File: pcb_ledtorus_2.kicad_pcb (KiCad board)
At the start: 4 copper layers, 149 x 149 mm, 277 parts, among them P1 CONN_02X04, P2 CONN_6, P3 MICRO-SD, P4 CONN_2, P5 KNUSB, P6 CONN_12, U1 STM32F46X_LQFP176, U10 TLC5955, U11 TLC5955, U12 TLC5955, U13 TLC5955, U14 TLC5955, U15 TLC5955, U3 LP38691, U4 TLC5955, U5 TLC5955, U6 TLC5955, U7 TLC5955, U8 TLC5955, U9 TLC5955, X1 MA-505

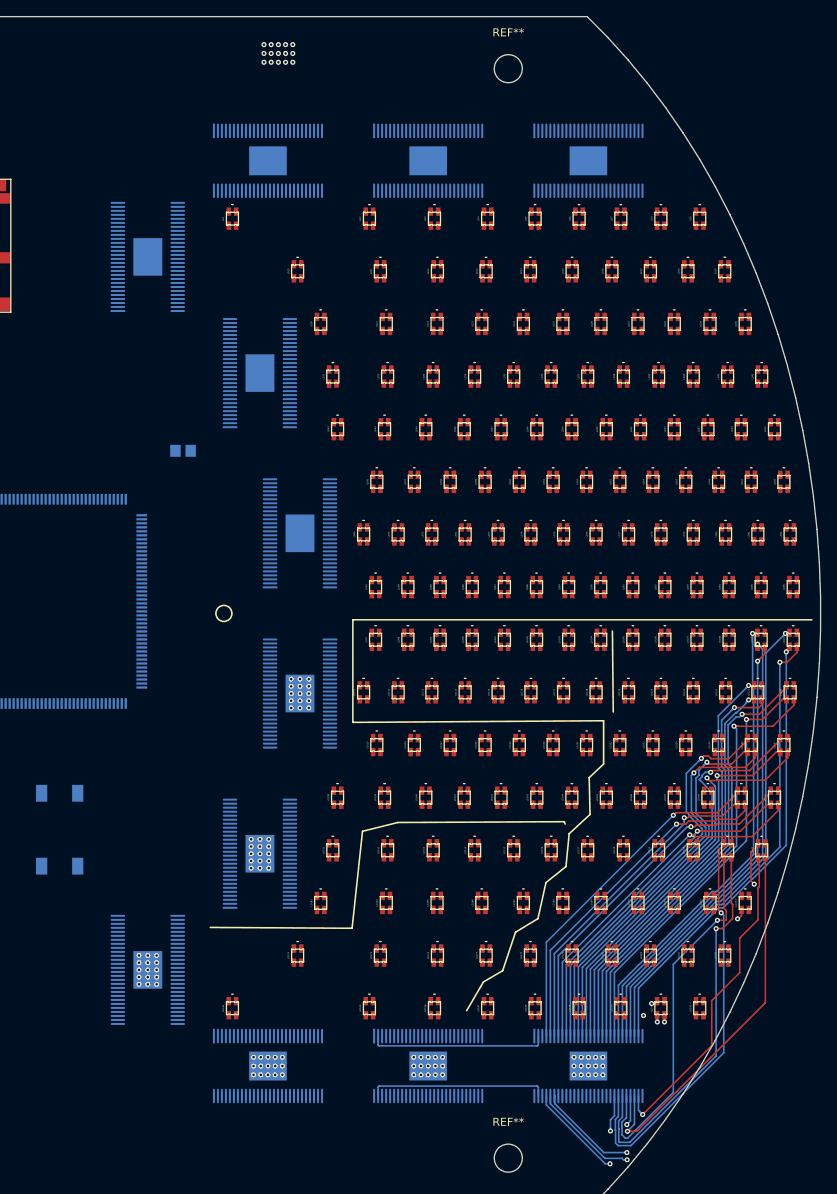
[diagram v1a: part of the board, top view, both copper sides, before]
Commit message: Good progress on LED routing.
Upper half now routed with 6/6 mil tracks/clearance.
Still need to fit 5V vias for all LEDs, hopefully vias can find room.
Looks promising - if everything works, lower half should be doable the
same way.
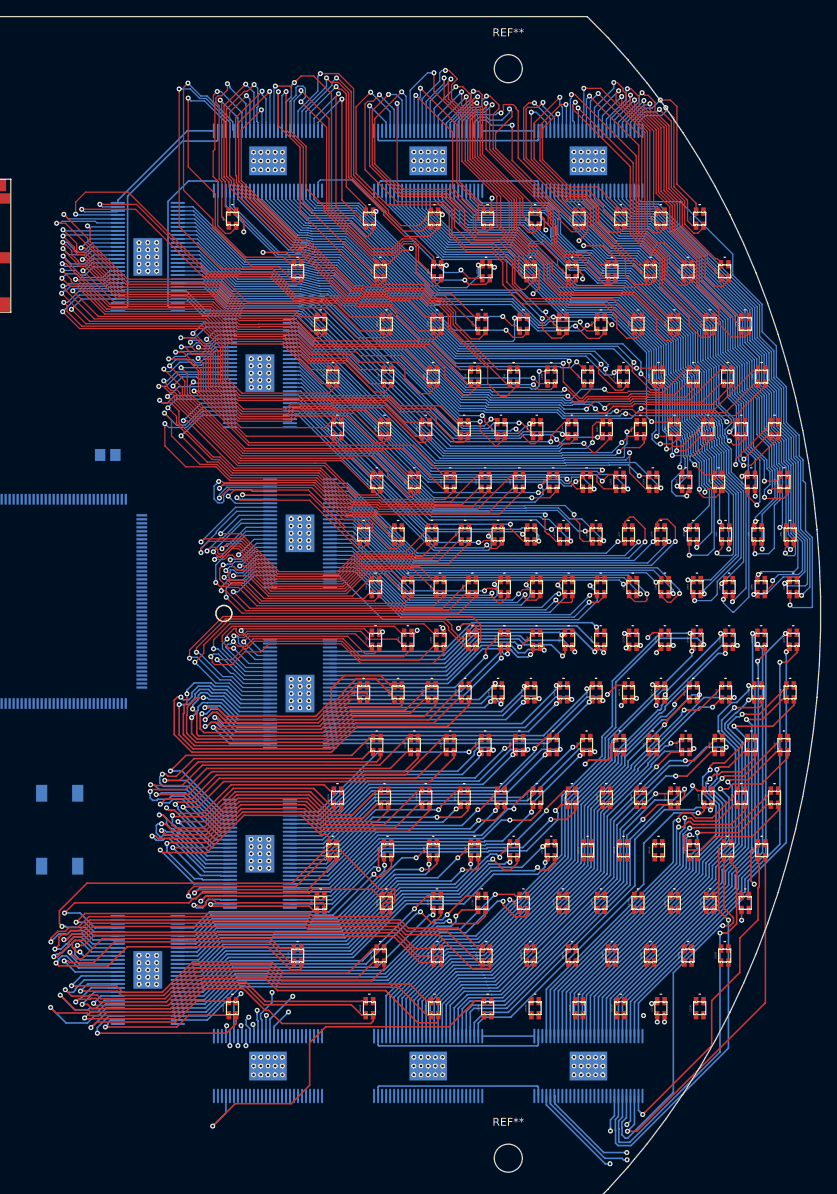
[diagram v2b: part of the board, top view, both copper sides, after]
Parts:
- moved C36 9.41 mm to (135.5, 130.2)
- turned U11 to 270 degrees
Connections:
- U11 pad 10: /LEDs/led140b -> /LEDs/led130b
- U11 pad 11: /LEDs/led140r -> /LEDs/led130r
- U11 pad 12: /LEDs/led140g -> /LEDs/led130g
- U11 pad 13: /LEDs/led139b -> /LEDs/led131b
- U11 pad 14: /LEDs/led139r -> /LEDs/led131r
- U11 pad 15: /LEDs/led139g -> /LEDs/led131g
- U11 pad 16: /LEDs/led138b -> /LEDs/led141b
- U11 pad 17: /LEDs/led138r -> /LEDs/led141r
- U11 pad 18: /LEDs/led138g -> /LEDs/led141g
- U11 pad 19: /LEDs/led127b -> /LEDs/led142b
- U11 pad 20: /LEDs/led127r -> /LEDs/led142r
- U11 pad 21: /LEDs/led127g -> /LEDs/led142g
- U11 pad 22: /LEDs/led126b -> /LEDs/led143b
- U11 pad 23: /LEDs/led126r -> /LEDs/led143r
- U11 pad 24: /LEDs/led126g -> /LEDs/led143g
- U11 pad 25: /LEDs/led125b -> /LEDs/led144b
- U11 pad 26: /LEDs/led125r -> /LEDs/led144r
- U11 pad 27: /LEDs/led125g -> /LEDs/led144g
- U11 pad 30: /LEDs/led128g -> /LEDs/led163g
- U11 pad 31: /LEDs/led128r -> /LEDs/led163r
- U11 pad 32: /LEDs/led128b -> /LEDs/led163b
- U11 pad 33: /LEDs/led129g -> /LEDs/led151g
- U11 pad 34: /LEDs/led129r -> /LEDs/led151r
- U11 pad 35: /LEDs/led129b -> /LEDs/led151b
- U11 pad 36: /LEDs/led130g -> /LEDs/led140g
- U11 pad 37: /LEDs/led130r -> /LEDs/led140r
- U11 pad 38: /LEDs/led130b -> /LEDs/led140b
- U11 pad 39: /LEDs/led131g -> /LEDs/led139g
- U11 pad 4: /LEDs/led163b -> /LEDs/led128b
- U11 pad 40: /LEDs/led131r -> /LEDs/led139r
- U11 pad 41: /LEDs/led131b -> /LEDs/led139b
- U11 pad 42: /LEDs/led141g -> /LEDs/led138g
- U11 pad 43: /LEDs/led141r -> /LEDs/led138r
- U11 pad 44: /LEDs/led141b -> /LEDs/led138b
- U11 pad 45: /LEDs/led142g -> /LEDs/led127g
- U11 pad 46: /LEDs/led142r -> /LEDs/led127r
- U11 pad 47: /LEDs/led142b -> /LEDs/led127b
- U11 pad 48: /LEDs/led143g -> /LEDs/led126g
- U11 pad 49: /LEDs/led143r -> /LEDs/led126r
- U11 pad 5: /LEDs/led163r -> /LEDs/led128r
- U11 pad 50: /LEDs/led143b -> /LEDs/led126b
- U11 pad 51: /LEDs/led144g -> /LEDs/led125g
- U11 pad 52: /LEDs/led144r -> /LEDs/led125r
- U11 pad 53: /LEDs/led144b -> /LEDs/led125b
- U11 pad 6: /LEDs/led163g -> /LEDs/led128g
- U11 pad 7: /LEDs/led151b -> /LEDs/led129b
- U11 pad 8: /LEDs/led151r -> /LEDs/led129r
- U11 pad 9: /LEDs/led151g -> /LEDs/led129g
- U12 pad 30: /LEDs/led186g -> /LEDs/led184g
- U12 pad 31: /LEDs/led186r -> /LEDs/led184r
- U12 pad 32: /LEDs/led186b -> /LEDs/led184b
- U12 pad 36: /LEDs/led184g -> /LEDs/led186g
- U12 pad 37: /LEDs/led184r -> /LEDs/led186r
- U12 pad 38: /LEDs/led184b -> /LEDs/led186b
- U12 pad 39: /LEDs/led174g -> /LEDs/led175g
- U12 pad 40: /LEDs/led174r -> /LEDs/led175r
- U12 pad 41: /LEDs/led174b -> /LEDs/led175b
- U12 pad 42: /LEDs/led175g -> /LEDs/led174g
- U12 pad 43: /LEDs/led175r -> /LEDs/led174r
- U12 pad 44: /LEDs/led175b -> /LEDs/led174b
- U13 pad 10: /LEDs/led132b -> /LEDs/led119b
- U13 pad 11: /LEDs/led132r -> /LEDs/led119r
- U13 pad 12: /LEDs/led132g -> /LEDs/led119g
- U13 pad 13: /LEDs/led133b -> /LEDs/led120b
- U13 pad 14: /LEDs/led133r -> /LEDs/led120r
- U13 pad 15: /LEDs/led133g -> /LEDs/led120g
- U13 pad 16: /LEDs/led119b -> /LEDs/led132b
- U13 pad 17: /LEDs/led119r -> /LEDs/led132r
- U13 pad 18: /LEDs/led119g -> /LEDs/led132g
- U13 pad 19: /LEDs/led120b -> /LEDs/led133b
- U13 pad 20: /LEDs/led120r -> /LEDs/led133r
- U13 pad 21: /LEDs/led120g -> /LEDs/led133g
- U13 pad 22: /LEDs/led105b -> /LEDs/led145b
- U13 pad 23: /LEDs/led105r -> /LEDs/led145r
- U13 pad 24: /LEDs/led105g -> /LEDs/led145g
- U13 pad 25: /LEDs/led106b -> /LEDs/led146b
- U13 pad 26: /LEDs/led106r -> /LEDs/led146r
- U13 pad 27: /LEDs/led106g -> /LEDs/led146g
- U13 pad 4: /LEDs/led145b -> /LEDs/led105b
- U13 pad 5: /LEDs/led145r -> /LEDs/led105r
- U13 pad 6: /LEDs/led145g -> /LEDs/led105g
- U13 pad 7: /LEDs/led146b -> /LEDs/led106b
- U13 pad 8: /LEDs/led146r -> /LEDs/led106r
- U13 pad 9: /LEDs/led146g -> /LEDs/led106g
- U14 pad 10: /LEDs/led134b -> /LEDs/led121b
- U14 pad 11: /LEDs/led134r -> /LEDs/led121r
- U14 pad 12: /LEDs/led134g -> /LEDs/led121g
- U14 pad 13: /LEDs/led135b -> /LEDs/led122b
- U14 pad 14: /LEDs/led135r -> /LEDs/led122r
- U14 pad 15: /LEDs/led135g -> /LEDs/led122g
- U14 pad 16: /LEDs/led121b -> /LEDs/led134b
- U14 pad 17: /LEDs/led121r -> /LEDs/led134r
- U14 pad 18: /LEDs/led121g -> /LEDs/led134g
- U14 pad 19: /LEDs/led122b -> /LEDs/led135b
- U14 pad 20: /LEDs/led122r -> /LEDs/led135r
- U14 pad 21: /LEDs/led122g -> /LEDs/led135g
- U14 pad 22: /LEDs/led107b -> /LEDs/led147b
- U14 pad 23: /LEDs/led107r -> /LEDs/led147r
- U14 pad 24: /LEDs/led107g -> /LEDs/led147g
- U14 pad 25: /LEDs/led108b -> /LEDs/led148b
- U14 pad 26: /LEDs/led108r -> /LEDs/led148r
- U14 pad 27: /LEDs/led108g -> /LEDs/led148g
- U14 pad 4: /LEDs/led147b -> /LEDs/led107b
- U14 pad 5: /LEDs/led147r -> /LEDs/led107r
- U14 pad 6: /LEDs/led147g -> /LEDs/led107g
- U14 pad 7: /LEDs/led148b -> /LEDs/led108b
- U14 pad 8: /LEDs/led148r -> /LEDs/led108r
- U14 pad 9: /LEDs/led148g -> /LEDs/led108g
- U4 pad 10: /LEDs/led3b -> /LEDs/led4b
- U4 pad 11: /LEDs/led3r -> /LEDs/led4r
- U4 pad 12: /LEDs/led3g -> /LEDs/led4g
- U4 pad 13: /LEDs/led4b -> /LEDs/led28b
- U4 pad 14: /LEDs/led4r -> /LEDs/led28r
- U4 pad 15: /LEDs/led4g -> /LEDs/led28g
- U4 pad 16: /LEDs/led5b -> /LEDs/led15b
- U4 pad 17: /LEDs/led5r -> /LEDs/led15r
- U4 pad 18: /LEDs/led5g -> /LEDs/led15g
- U4 pad 19: /LEDs/led6b -> /LEDs/led5b
- U4 pad 20: /LEDs/led6r -> /LEDs/led5r
- U4 pad 21: /LEDs/led6g -> /LEDs/led5g
- U4 pad 22: /LEDs/led7b -> /LEDs/led16b
- U4 pad 23: /LEDs/led7r -> /LEDs/led16r
- U4 pad 24: /LEDs/led7g -> /LEDs/led16g
- U4 pad 25: /LEDs/led8b -> /LEDs/led6b
- U4 pad 26: /LEDs/led8r -> /LEDs/led6r
- U4 pad 27: /LEDs/led8g -> /LEDs/led6g
- U4 pad 30: /LEDs/led16g -> /LEDs/led94g
- U4 pad 31: /LEDs/led16r -> /LEDs/led94r
- U4 pad 32: /LEDs/led16b -> /LEDs/led94b
- U4 pad 33: /LEDs/led15g -> /LEDs/led93g
- U4 pad 34: /LEDs/led15r -> /LEDs/led93r
- U4 pad 35: /LEDs/led15b -> /LEDs/led93b
- U4 pad 36: /LEDs/led14g -> /LEDs/led80g
- U4 pad 37: /LEDs/led14r -> /LEDs/led80r
- U4 pad 38: /LEDs/led14b -> /LEDs/led80b
- U4 pad 39: /LEDs/led13g -> /LEDs/led79g
- U4 pad 4: /LEDs/led1b -> /LEDs/led27b
- U4 pad 40: /LEDs/led13r -> /LEDs/led79r
- U4 pad 41: /LEDs/led13b -> /LEDs/led79b
- U4 pad 42: /LEDs/led12g -> /LEDs/led66g
- U4 pad 43: /LEDs/led12r -> /LEDs/led66r
- U4 pad 44: /LEDs/led12b -> /LEDs/led66b
- U4 pad 45: /LEDs/led11g -> /LEDs/led65g
- U4 pad 46: /LEDs/led11r -> /LEDs/led65r
- U4 pad 47: /LEDs/led11b -> /LEDs/led65b
- U4 pad 48: /LEDs/led10g -> /LEDs/led53g
- U4 pad 49: /LEDs/led10r -> /LEDs/led53r
- U4 pad 5: /LEDs/led1r -> /LEDs/led27r
- U4 pad 50: /LEDs/led10b -> /LEDs/led53b
- U4 pad 51: /LEDs/led9g -> /LEDs/led52g
- U4 pad 52: /LEDs/led9r -> /LEDs/led52r
- U4 pad 53: /LEDs/led9b -> /LEDs/led52b
- U4 pad 6: /LEDs/led1g -> /LEDs/led27g
- U4 pad 7: /LEDs/led2b -> /LEDs/led14b
- U4 pad 8: /LEDs/led2r -> /LEDs/led14r
- U4 pad 9: /LEDs/led2g -> /LEDs/led14g
- U5 pad 10: /LEDs/led16b -> /LEDs/led29b
- U5 pad 11: /LEDs/led16r -> /LEDs/led29r
- U5 pad 12: /LEDs/led16g -> /LEDs/led29g
- U5 pad 13: /LEDs/led7b -> /LEDs/led18b
- U5 pad 14: /LEDs/led7r -> /LEDs/led18r
- U5 pad 15: /LEDs/led7g -> /LEDs/led18g
- U5 pad 16: /LEDs/led17b -> /LEDs/led8b
- U5 pad 17: /LEDs/led17r -> /LEDs/led8r
- U5 pad 18: /LEDs/led17g -> /LEDs/led8g
- U5 pad 19: /LEDs/led18b -> /LEDs/led30b
- U5 pad 20: /LEDs/led18r -> /LEDs/led30r
- U5 pad 21: /LEDs/led18g -> /LEDs/led30g
- U5 pad 22: /LEDs/led9b -> /LEDs/led19b
- U5 pad 23: /LEDs/led9r -> /LEDs/led19r
- U5 pad 24: /LEDs/led9g -> /LEDs/led19g
- U5 pad 25: /LEDs/led19b -> /LEDs/led9b
- U5 pad 26: /LEDs/led19r -> /LEDs/led9r
- U5 pad 27: /LEDs/led19g -> /LEDs/led9g
- U5 pad 30: /LEDs/led42g -> /LEDs/led96g
- U5 pad 31: /LEDs/led42r -> /LEDs/led96r
- U5 pad 32: /LEDs/led42b -> /LEDs/led96b
- U5 pad 33: /LEDs/led30g -> /LEDs/led95g
- U5 pad 34: /LEDs/led30r -> /LEDs/led95r
- U5 pad 35: /LEDs/led30b -> /LEDs/led95b
- U5 pad 36: /LEDs/led41g -> /LEDs/led82g
- U5 pad 37: /LEDs/led41r -> /LEDs/led82r
- U5 pad 38: /LEDs/led41b -> /LEDs/led82b
- U5 pad 39: /LEDs/led29g -> /LEDs/led81g
- U5 pad 4: /LEDs/led15b -> /LEDs/led17b
- U5 pad 40: /LEDs/led29r -> /LEDs/led81r
- U5 pad 41: /LEDs/led29b -> /LEDs/led81b
- U5 pad 42: /LEDs/led40g -> /LEDs/led68g
- U5 pad 43: /LEDs/led40r -> /LEDs/led68r
- U5 pad 44: /LEDs/led40b -> /LEDs/led68b
- U5 pad 45: /LEDs/led28g -> /LEDs/led67g
- U5 pad 46: /LEDs/led28r -> /LEDs/led67r
- U5 pad 47: /LEDs/led28b -> /LEDs/led67b
- U5 pad 48: /LEDs/led39g -> /LEDs/led55g
- U5 pad 49: /LEDs/led39r -> /LEDs/led55r
- U5 pad 5: /LEDs/led15r -> /LEDs/led17r
- U5 pad 50: /LEDs/led39b -> /LEDs/led55b
- U5 pad 51: /LEDs/led27g -> /LEDs/led54g
- U5 pad 52: /LEDs/led27r -> /LEDs/led54r
- U5 pad 53: /LEDs/led27b -> /LEDs/led54b
- U5 pad 6: /LEDs/led15g -> /LEDs/led17g
- U5 pad 7: /LEDs/led6b -> /LEDs/led7b
- U5 pad 8: /LEDs/led6r -> /LEDs/led7r
- U5 pad 9: /LEDs/led6g -> /LEDs/led7g
- U6 pad 10: /LEDs/led35b -> /LEDs/led32b
- U6 pad 11: /LEDs/led35r -> /LEDs/led32r
- U6 pad 12: /LEDs/led35g -> /LEDs/led32g
- U6 pad 13: /LEDs/led36b -> /LEDs/led33b
- U6 pad 14: /LEDs/led36r -> /LEDs/led33r
- U6 pad 15: /LEDs/led36g -> /LEDs/led33g
- U6 pad 16: /LEDs/led37b -> /LEDs/led34b
- U6 pad 17: /LEDs/led37r -> /LEDs/led34r
- U6 pad 18: /LEDs/led37g -> /LEDs/led34g
- U6 pad 19: /LEDs/led38b -> /LEDs/led20b
- U6 pad 20: /LEDs/led38r -> /LEDs/led20r
- U6 pad 21: /LEDs/led38g -> /LEDs/led20g
- U6 pad 22: /LEDs/led39b -> /LEDs/led21b
- U6 pad 23: /LEDs/led39r -> /LEDs/led21r
- U6 pad 24: /LEDs/led39g -> /LEDs/led21g
- U6 pad 25: /LEDs/led40b -> /LEDs/led22b
- U6 pad 26: /LEDs/led40r -> /LEDs/led22r
- U6 pad 27: /LEDs/led40g -> /LEDs/led22g
- U6 pad 30: /LEDs/led48g -> /LEDs/led40g
- U6 pad 31: /LEDs/led48r -> /LEDs/led40r
- U6 pad 32: /LEDs/led48b -> /LEDs/led40b
- U6 pad 33: /LEDs/led47g -> /LEDs/led41g
- U6 pad 34: /LEDs/led47r -> /LEDs/led41r
- U6 pad 35: /LEDs/led47b -> /LEDs/led41b
- U6 pad 36: /LEDs/led46g -> /LEDs/led42g
- U6 pad 37: /LEDs/led46r -> /LEDs/led42r
- U6 pad 38: /LEDs/led46b -> /LEDs/led42b
- U6 pad 39: /LEDs/led45g -> /LEDs/led47g
- U6 pad 4: /LEDs/led31b -> /LEDs/led46b
- U6 pad 40: /LEDs/led45r -> /LEDs/led47r
- U6 pad 41: /LEDs/led45b -> /LEDs/led47b
- U6 pad 42: /LEDs/led44g -> /LEDs/led48g
- U6 pad 43: /LEDs/led44r -> /LEDs/led48r
- U6 pad 44: /LEDs/led44b -> /LEDs/led48b
- U6 pad 45: /LEDs/led43g -> /LEDs/led49g
- U6 pad 46: /LEDs/led43r -> /LEDs/led49r
- U6 pad 47: /LEDs/led43b -> /LEDs/led49b
- U6 pad 48: /LEDs/led42g -> /LEDs/led50g
- U6 pad 49: /LEDs/led42r -> /LEDs/led50r
- U6 pad 5: /LEDs/led31r -> /LEDs/led46r
- U6 pad 50: /LEDs/led42b -> /LEDs/led50b
- U6 pad 51: /LEDs/led41g -> /LEDs/led51g
- U6 pad 52: /LEDs/led41r -> /LEDs/led51r
- U6 pad 53: /LEDs/led41b -> /LEDs/led51b
- U6 pad 6: /LEDs/led31g -> /LEDs/led46g
- U6 pad 7: /LEDs/led34b -> /LEDs/led31b
- U6 pad 8: /LEDs/led34r -> /LEDs/led31r
- U6 pad 9: /LEDs/led34g -> /LEDs/led31g
- U7 pad 10: /LEDs/led51b -> /LEDs/led35b
- U7 pad 11: /LEDs/led51r -> /LEDs/led35r
- U7 pad 12: /LEDs/led51g -> /LEDs/led35g
- U7 pad 13: /LEDs/led52b -> /LEDs/led23b
- U7 pad 14: /LEDs/led52r -> /LEDs/led23r
- U7 pad 15: /LEDs/led52g -> /LEDs/led23g
- U7 pad 16: /LEDs/led53b -> /LEDs/led11b
- U7 pad 17: /LEDs/led53r -> /LEDs/led11r
- U7 pad 18: /LEDs/led53g -> /LEDs/led11g
- U7 pad 19: /LEDs/led54b -> /LEDs/led12b
- U7 pad 20: /LEDs/led54r -> /LEDs/led12r
- U7 pad 21: /LEDs/led54g -> /LEDs/led12g
- U7 pad 22: /LEDs/led55b -> /LEDs/led3b
- U7 pad 23: /LEDs/led55r -> /LEDs/led3r
- U7 pad 24: /LEDs/led55g -> /LEDs/led3g
- U7 pad 25: /LEDs/led56b -> /LEDs/led2b
- U7 pad 26: /LEDs/led56r -> /LEDs/led2r
- U7 pad 27: /LEDs/led56g -> /LEDs/led2g
- U7 pad 30: /LEDs/led64g -> /LEDs/led13g
- U7 pad 31: /LEDs/led64r -> /LEDs/led13r
- U7 pad 32: /LEDs/led64b -> /LEDs/led13b
- U7 pad 33: /LEDs/led63g -> /LEDs/led25g
- U7 pad 34: /LEDs/led63r -> /LEDs/led25r
- U7 pad 35: /LEDs/led63b -> /LEDs/led25b
- U7 pad 36: /LEDs/led62g -> /LEDs/led26g
- U7 pad 37: /LEDs/led62r -> /LEDs/led26r
- U7 pad 38: /LEDs/led62b -> /LEDs/led26b
- U7 pad 39: /LEDs/led61g -> /LEDs/led24g
- U7 pad 4: /LEDs/led49b -> /LEDs/led10b
- U7 pad 40: /LEDs/led61r -> /LEDs/led24r
- U7 pad 41: /LEDs/led61b -> /LEDs/led24b
- U7 pad 42: /LEDs/led60g -> /LEDs/led39g
- U7 pad 43: /LEDs/led60r -> /LEDs/led39r
- U7 pad 44: /LEDs/led60b -> /LEDs/led39b
- U7 pad 45: /LEDs/led59g -> /LEDs/led38g
- U7 pad 46: /LEDs/led59r -> /LEDs/led38r
- U7 pad 47: /LEDs/led59b -> /LEDs/led38b
- U7 pad 48: /LEDs/led58g -> /LEDs/led37g
- U7 pad 49: /LEDs/led58r -> /LEDs/led37r
- U7 pad 5: /LEDs/led49r -> /LEDs/led10r
- U7 pad 50: /LEDs/led58b -> /LEDs/led37b
- U7 pad 51: /LEDs/led57g -> /LEDs/led36g
- U7 pad 52: /LEDs/led57r -> /LEDs/led36r
- U7 pad 53: /LEDs/led57b -> /LEDs/led36b
- U7 pad 6: /LEDs/led49g -> /LEDs/led10g
- U7 pad 7: /LEDs/led50b -> /LEDs/led1b
- U7 pad 8: /LEDs/led50r -> /LEDs/led1r
- U7 pad 9: /LEDs/led50g -> /LEDs/led1g
- U8 pad 10: /LEDs/led67b -> /LEDs/led84b
- U8 pad 11: /LEDs/led67r -> /LEDs/led84r
- U8 pad 12: /LEDs/led67g -> /LEDs/led84g
- U8 pad 13: /LEDs/led68b -> /LEDs/led85b
- U8 pad 14: /LEDs/led68r -> /LEDs/led85r
- U8 pad 15: /LEDs/led68g -> /LEDs/led85g
- U8 pad 16: /LEDs/led69b -> /LEDs/led72b
- U8 pad 17: /LEDs/led69r -> /LEDs/led72r
- U8 pad 18: /LEDs/led69g -> /LEDs/led72g
- U8 pad 19: /LEDs/led70b -> /LEDs/led71b
- U8 pad 20: /LEDs/led70r -> /LEDs/led71r
- U8 pad 21: /LEDs/led70g -> /LEDs/led71g
- U8 pad 22: /LEDs/led71b -> /LEDs/led69b
- U8 pad 23: /LEDs/led71r -> /LEDs/led69r
- U8 pad 24: /LEDs/led71g -> /LEDs/led69g
- U8 pad 25: /LEDs/led72b -> /LEDs/led70b
- U8 pad 26: /LEDs/led72r -> /LEDs/led70r
- U8 pad 27: /LEDs/led72g -> /LEDs/led70g
- U8 pad 30: /LEDs/led80g -> /LEDs/led77g
- U8 pad 31: /LEDs/led80r -> /LEDs/led77r
- U8 pad 32: /LEDs/led80b -> /LEDs/led77b
- U8 pad 33: /LEDs/led79g -> /LEDs/led78g
- U8 pad 34: /LEDs/led79r -> /LEDs/led78r
- U8 pad 35: /LEDs/led79b -> /LEDs/led78b
- U8 pad 36: /LEDs/led78g -> /LEDs/led92g
- U8 pad 37: /LEDs/led78r -> /LEDs/led92r
- U8 pad 38: /LEDs/led78b -> /LEDs/led92b
- U8 pad 39: /LEDs/led77g -> /LEDs/led91g
- U8 pad 4: /LEDs/led65b -> /LEDs/led86b
- U8 pad 40: /LEDs/led77r -> /LEDs/led91r
- U8 pad 41: /LEDs/led77b -> /LEDs/led91b
- U8 pad 42: /LEDs/led76g -> /LEDs/led87g
- U8 pad 43: /LEDs/led76r -> /LEDs/led87r
- U8 pad 44: /LEDs/led76b -> /LEDs/led87b
- U8 pad 45: /LEDs/led75g -> /LEDs/led88g
- U8 pad 46: /LEDs/led75r -> /LEDs/led88r
- U8 pad 47: /LEDs/led75b -> /LEDs/led88b
- U8 pad 48: /LEDs/led74g -> /LEDs/led89g
- U8 pad 49: /LEDs/led74r -> /LEDs/led89r
- U8 pad 5: /LEDs/led65r -> /LEDs/led86r
- U8 pad 50: /LEDs/led74b -> /LEDs/led89b
- U8 pad 51: /LEDs/led73g -> /LEDs/led90g
- U8 pad 52: /LEDs/led73r -> /LEDs/led90r
- U8 pad 53: /LEDs/led73b -> /LEDs/led90b
- U8 pad 6: /LEDs/led65g -> /LEDs/led86g
- U8 pad 7: /LEDs/led66b -> /LEDs/led83b
- U8 pad 8: /LEDs/led66r -> /LEDs/led83r
- U8 pad 9: /LEDs/led66g -> /LEDs/led83g
- U9 pad 10: /LEDs/led83b -> /LEDs/led58b
- U9 pad 11: /LEDs/led83r -> /LEDs/led58r
- U9 pad 12: /LEDs/led83g -> /LEDs/led58g
- U9 pad 13: /LEDs/led84b -> /LEDs/led56b
- U9 pad 14: /LEDs/led84r -> /LEDs/led56r
- U9 pad 15: /LEDs/led84g -> /LEDs/led56g
- U9 pad 16: /LEDs/led85b -> /LEDs/led57b
- U9 pad 17: /LEDs/led85r -> /LEDs/led57r
- U9 pad 18: /LEDs/led85g -> /LEDs/led57g
- U9 pad 19: /LEDs/led86b -> /LEDs/led43b
- U9 pad 20: /LEDs/led86r -> /LEDs/led43r
- U9 pad 21: /LEDs/led86g -> /LEDs/led43g
- U9 pad 22: /LEDs/led87b -> /LEDs/led44b
- U9 pad 23: /LEDs/led87r -> /LEDs/led44r
- U9 pad 24: /LEDs/led87g -> /LEDs/led44g
- U9 pad 25: /LEDs/led88b -> /LEDs/led45b
- U9 pad 26: /LEDs/led88r -> /LEDs/led45r
- U9 pad 27: /LEDs/led88g -> /LEDs/led45g
- U9 pad 30: /LEDs/led96g -> /LEDs/led64g
- U9 pad 31: /LEDs/led96r -> /LEDs/led64r
- U9 pad 32: /LEDs/led96b -> /LEDs/led64b
- U9 pad 33: /LEDs/led95g -> /LEDs/led63g
- U9 pad 34: /LEDs/led95r -> /LEDs/led63r
- U9 pad 35: /LEDs/led95b -> /LEDs/led63b
- U9 pad 36: /LEDs/led94g -> /LEDs/led62g
- U9 pad 37: /LEDs/led94r -> /LEDs/led62r
- U9 pad 38: /LEDs/led94b -> /LEDs/led62b
- U9 pad 39: /LEDs/led93g -> /LEDs/led61g
- U9 pad 4: /LEDs/led81b -> /LEDs/led60b
- U9 pad 40: /LEDs/led93r -> /LEDs/led61r
- U9 pad 41: /LEDs/led93b -> /LEDs/led61b
- U9 pad 42: /LEDs/led92g -> /LEDs/led76g
- U9 pad 43: /LEDs/led92r -> /LEDs/led76r
- U9 pad 44: /LEDs/led92b -> /LEDs/led76b
- U9 pad 45: /LEDs/led91g -> /LEDs/led75g
- U9 pad 46: /LEDs/led91r -> /LEDs/led75r
- U9 pad 47: /LEDs/led91b -> /LEDs/led75b
- U9 pad 48: /LEDs/led90g -> /LEDs/led74g
- U9 pad 49: /LEDs/led90r -> /LEDs/led74r
- U9 pad 5: /LEDs/led81r -> /LEDs/led60r
- U9 pad 50: /LEDs/led90b -> /LEDs/led74b
- U9 pad 51: /LEDs/led89g -> /LEDs/led73g
- U9 pad 52: /LEDs/led89r -> /LEDs/led73r
- U9 pad 53: /LEDs/led89b -> /LEDs/led73b
- U9 pad 6: /LEDs/led81g -> /LEDs/led60g
- U9 pad 7: /LEDs/led82b -> /LEDs/led59b
- U9 pad 8: /LEDs/led82r -> /LEDs/led59r
- U9 pad 9: /LEDs/led82g -> /LEDs/led59g
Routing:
- net /LEDs/led106b: track 0.00 -> 89.5 mm, vias 0 -> 2
- net /LEDs/led105r: track 0.00 -> 88.0 mm, vias 0 -> 2
- net /LEDs/led106r: track 0.00 -> 87.3 mm, vias 0 -> 2
- net /LEDs/led106g: track 0.00 -> 87.3 mm, vias 0 -> 2
- net /LEDs/led105b: track 0.00 -> 84.6 mm, vias 0 -> 2
- net /LEDs/led42r: track 0.00 -> 84.6 mm, vias 0 -> 1
- net /LEDs/led42b: track 0.00 -> 84.3 mm, vias 0 -> 1
- net /LEDs/led42g: track 0.00 -> 83.6 mm, vias 0 -> 1
- net /LEDs/led105g: track 0.00 -> 83.0 mm, vias 0 -> 2
- net /LEDs/led41r: track 0.00 -> 80.6 mm, vias 0 -> 1
- net /LEDs/led120b: track 0.00 -> 80.3 mm, vias 0 -> 2
- net /LEDs/led120r: track 0.00 -> 80.2 mm, vias 0 -> 2
- net /LEDs/led41b: track 0.00 -> 79.6 mm, vias 0 -> 1
- net /LEDs/led41g: track 0.00 -> 79.3 mm, vias 0 -> 1
- net /LEDs/led119b: track 0.00 -> 78.6 mm, vias 0 -> 2
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- added copper zone on In1.Cu, net +5V
- added copper zone on In2.Cu, net GND
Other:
- net class Inner: clearance 0.2032 -> 0.254; trace_width 0.254 -> 0.2032

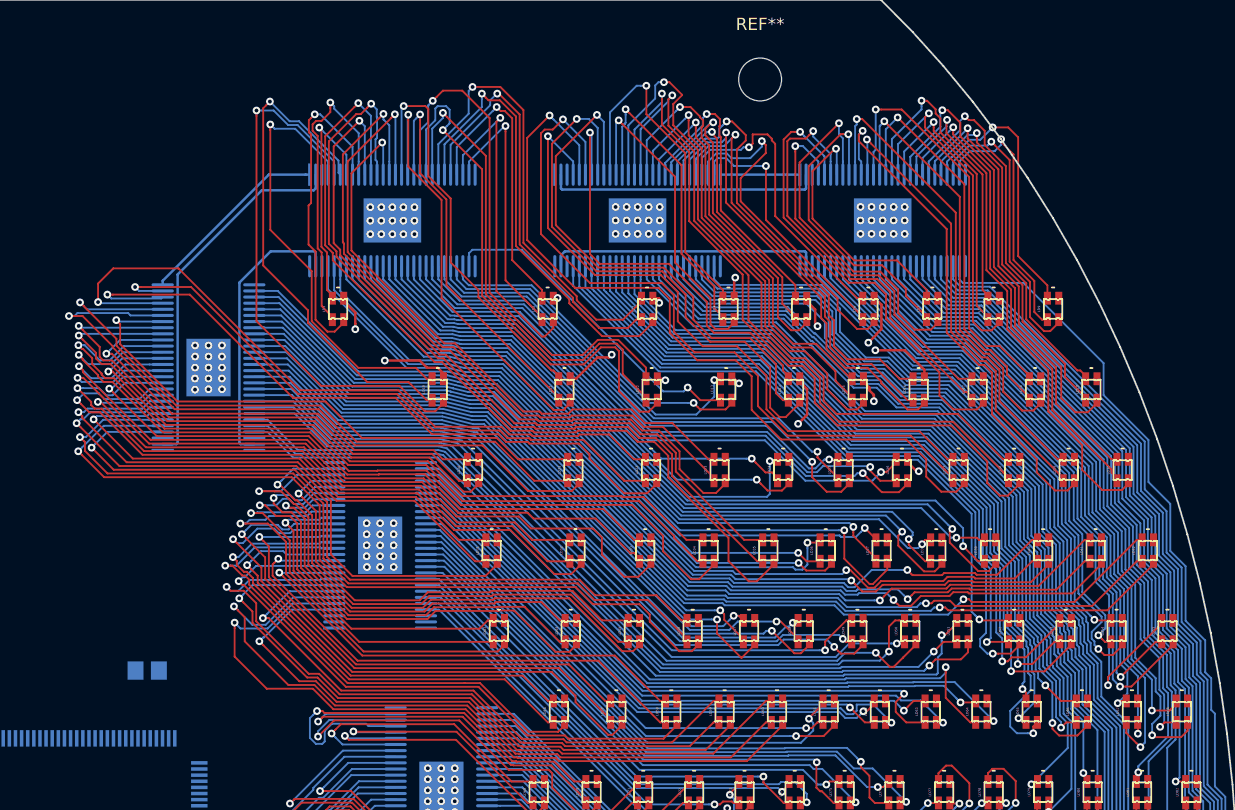
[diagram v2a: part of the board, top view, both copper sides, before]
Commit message: Some routing of LEDs VCC.
It's tight, but it looks possible.
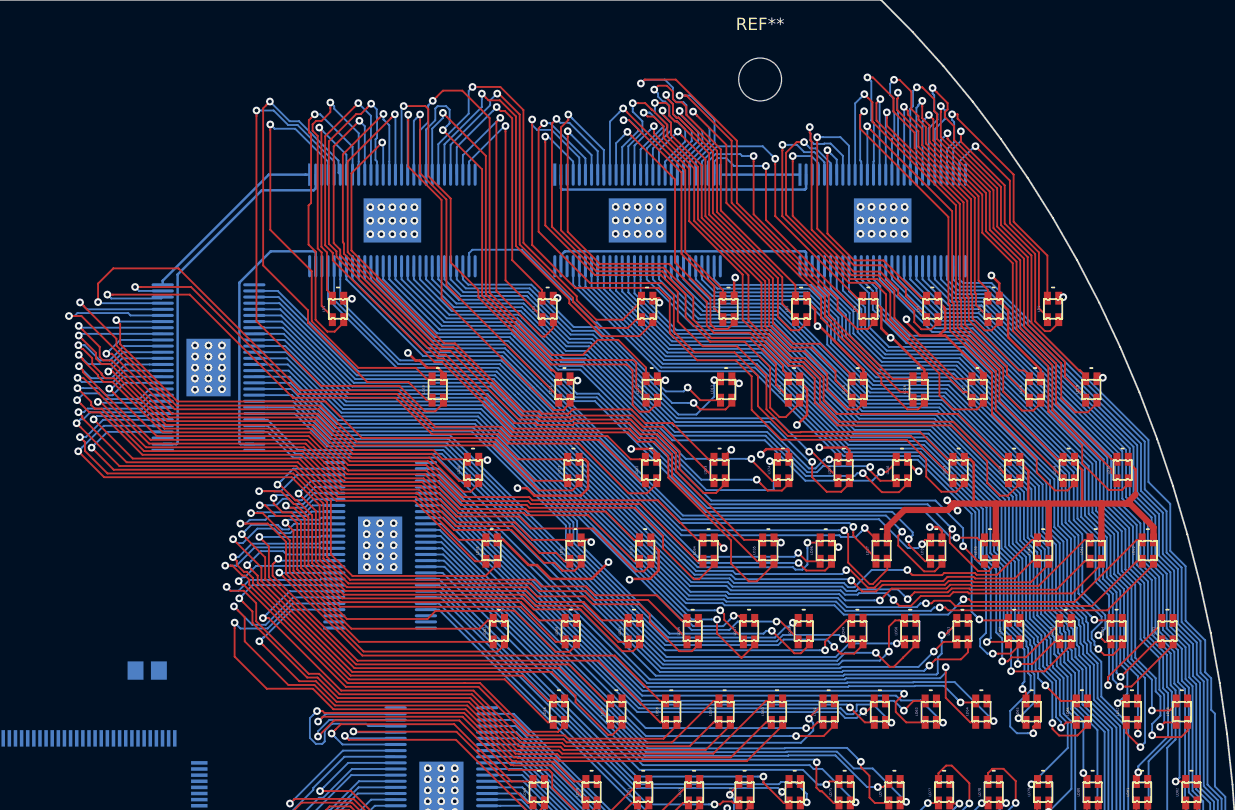
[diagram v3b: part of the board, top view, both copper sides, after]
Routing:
- net +5V: track 42.8 -> 154.8 mm, vias 18 -> 35
- net /LEDs/led16b: track 36.7 -> 48.5 mm
- net /LEDs/led16g: track 34.7 -> 42.2 mm
- net /LEDs/led5b: track 24.8 -> 32.0 mm
- net /LEDs/led5r: track 27.8 -> 33.5 mm
- net /LEDs/led28r: track 60.1 -> 54.8 mm
- net /LEDs/led19b: track 31.9 -> 36.7 mm
- net /LEDs/led5g: track 23.0 -> 27.5 mm
- net /LEDs/led18b: track 34.4 -> 38.7 mm
- net /LEDs/led6r: track 28.8 -> 24.5 mm
- net /LEDs/led4b: track 28.9 -> 24.7 mm
- net /LEDs/led19r: track 34.0 -> 37.9 mm
- net /LEDs/led30b: track 41.2 -> 45.0 mm
- net /LEDs/led8b: track 25.7 -> 29.3 mm
- net /LEDs/led18r: track 35.0 -> 38.7 mm
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
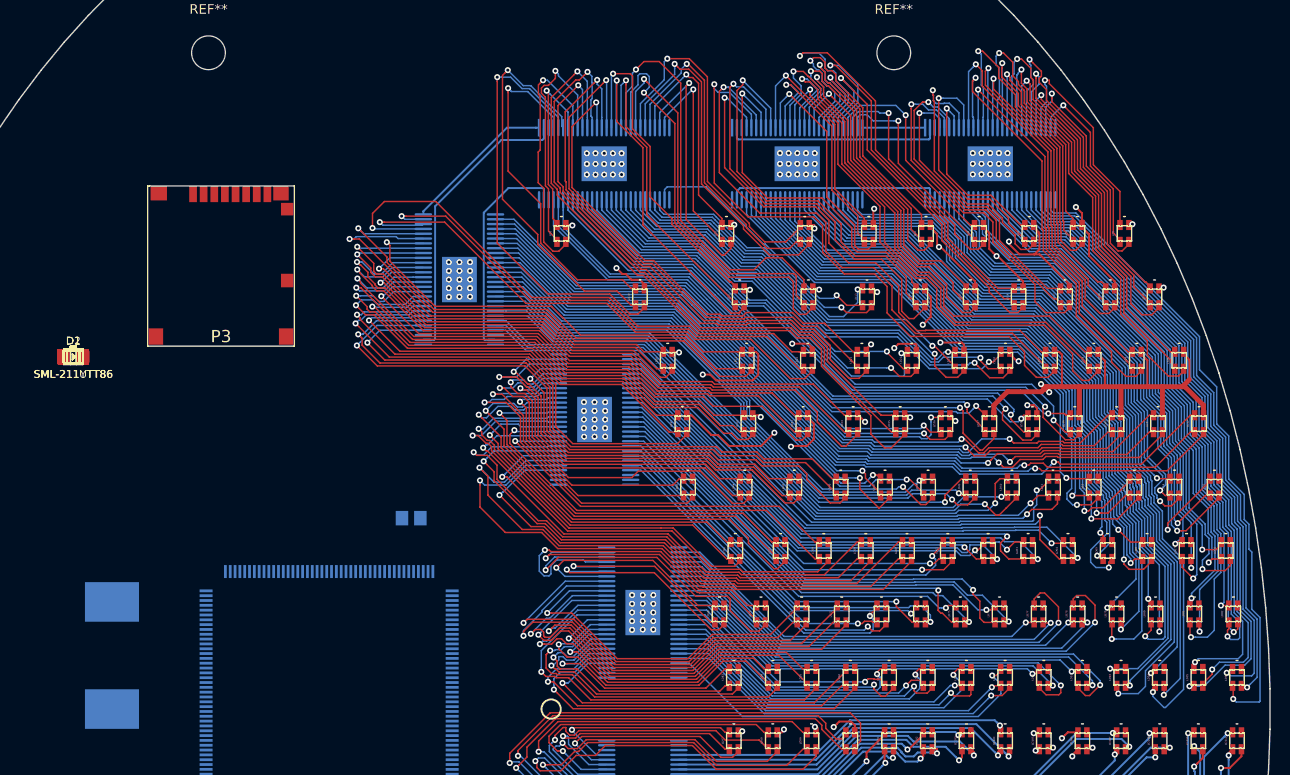
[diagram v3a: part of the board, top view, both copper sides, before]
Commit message: First reasonably complete routing of upper half of LEDs.
All LEDs have vias to power plane now. And TLCs have power and de-coupling.
Everything seems to fit, just.
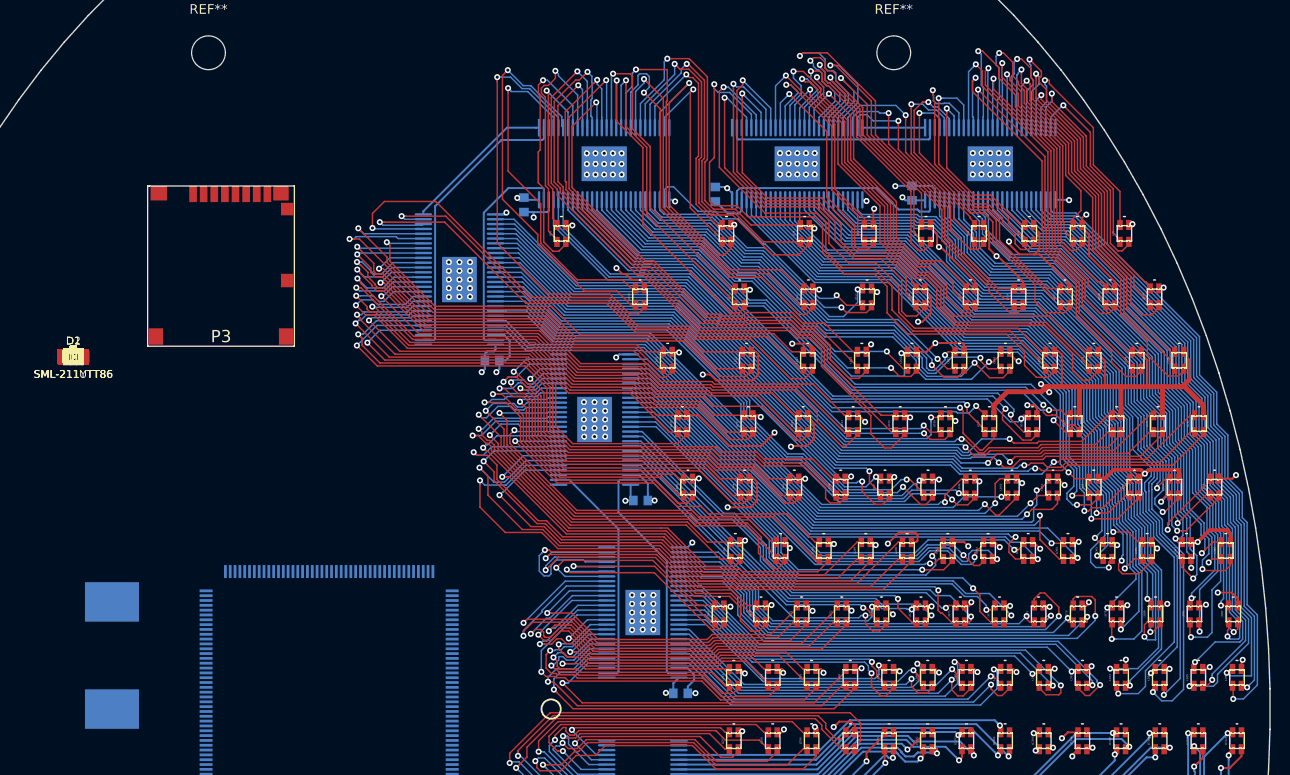
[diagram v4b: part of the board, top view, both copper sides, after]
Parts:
- C34, C35, C37, C38, C39: footprint w_smd_cap:c_0805 -> w_smd_cap:c_0603; moved to B.Cu
- C36, C40, C41, C42, C43, C44, C45: footprint w_smd_cap:c_0805 -> w_smd_cap:c_0603
- moved C35 88.5 mm to (187.4, 96.5), turned to 90 degrees
- moved C38 71.9 mm to (163.4, 148.4)
- moved C34 68.6 mm to (167.0, 96.7), turned to 270 degrees
- moved C39 60.6 mm to (159.3, 128.4)
- moved C37 49.3 mm to (147.2, 97.8), turned to 270 degrees
- moved C36 18.4 mm to (143.9, 113.9)
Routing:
- net +5V: track 154.8 -> 222.8 mm, vias 35 -> 85
- net +3V3: track 0.00 -> 29.6 mm, vias 0 -> 5
- net /LEDs/gsclk3: track 0.00 -> 24.4 mm
- net /LEDs/sclk3: track 0.00 -> 24.4 mm
- net GND: track 0.00 -> 23.7 mm, vias 180 -> 192
- net /LEDs/led62b: track 44.1 -> 46.2 mm
- net /LEDs/led12b: track 43.8 -> 41.7 mm
- net /LEDs/led90b: track 40.2 -> 38.3 mm
- net /LEDs/led25b: track 40.4 -> 42.2 mm
- net /LEDs/led27r: track 65.2 -> 67.0 mm
- net /LEDs/led54b: track 43.2 -> 44.9 mm
- net /LEDs/led76r: track 48.3 -> 50.0 mm
- net /LEDs/led12r: track 44.2 -> 42.5 mm
- net /LEDs/led72b: track 41.9 -> 40.2 mm
- net /LEDs/led72r: track 45.3 -> 43.6 mm
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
